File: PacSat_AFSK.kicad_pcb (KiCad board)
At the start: 6 copper layers, 92 x 92 mm, 308 parts, among them J10 2118718-2, J11 Molex 73251-1153, J2 CONN_02X05, J3 2118714-2, J4 2118714-2, J5 2118714-2, J6 2118714-2, J7 2118714-2, J8 Molex 73251-1153, J9 2118714-2, P10 CONUFL001-SMD-T, P11 CONUFL001-SMD-T, P12 CONUFL001-SMD-T, P13 CONUFL001-SMD-T, P14 Conn_04x26_Pin, P2 CONUFL001-SMD-T, P3 CONUFL001-SMD-T, P4 CONUFL001-SMD-T, P5 CONUFL001-SMD-T, P6 CONUFL001-SMD-T, P7 CONUFL001-SMD-T, P9 CONUFL001-SMD-T, Q2 BSS138, Q3 DMP2037U, Q4 DMP2037U, Q5 DMP2037U, Q6 DMP2037U, Q7 DMP2037U, U10 MAX4495AAUT, U11 MAX4495AAUT, U12 MAX31331TETB+, U13 AS1016204-0108X0PWAY, U14 TCAN1044ADDFRQ1, U15 AX5043, U17 AX5043, U19 AX5043, U2 TMS570LS0914PGE, U21 AX5043, U23 AX5043, U25 QPL9547, U26 RBP-140+, U27 TQP7M9106, U28 ADL5501AKSZ-R2, U29 ADL5501AKSZ-R2, U3 CDCLVC1106, U4 TPSM828302ARDSR, U5 LP3962EMP-3.3/NOPB, U6 STWD100NYWY3F, U8 MP5073GG-P, U9 MAX4495AAUT, Y2 O 16,0-JT22CT-A-P-3,3-LF, Y3 32.768kHz

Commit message: Remove the ground from KELVIN_GND
From reading the data sheet, it appears it is not supposed to be
connected.

Signed-off-by: Corey Minyard <corey@minyard.net>
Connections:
- U2 pad 19: GND -> unconnected-(U2-KELVIN_GND-Pad19)
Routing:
- net GND: track 291.5 -> 289.5 mm, vias 384 -> 383
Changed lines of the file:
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@@
 	(net 375 "AX5043_SEL1_N")
 	(net 376 "AX5043_SEL_TX_N")
+	(net 377 "unconnected-(U2-KELVIN_GND-Pad19)")
 	(footprint "Capacitor_SMD:C_0603_1608Metric_Pad1.08x0.95mm_HandSolder"
 		(layer "F.Cu")
@@
 			(size 1.6 0.3)
 			(layers "F.Cu" "F.Mask" "F.Paste")
-			(net 1 "GND")
+			(net 377 "unconnected-(U2-KELVIN_GND-Pad19)")
 			(pinfunction "KELVIN_GND")
-			(pintype "passive")
+			(pintype "passive+no_connect")
 		)
 		(pad "20" smd rect
@@
 	)
 	(segment
-		(start 190.758 77.715)
-		(end 190.758 79.7012)
-		(width 0.3048)
-		(layer "F.Cu")
-		(net 1)
-	)
-	(segment
 		(start 206.64 99.25)
 		(end 206.44 99.05)
@@
 		(size 0.508)
 		(drill 0.3048)
-		(layers "F.Cu" "B.Cu")
-		(net 1)
-	)
-	(via
-		(at 190.758 79.7012)
-		(size 0.508)
-		(drill 0.3048)

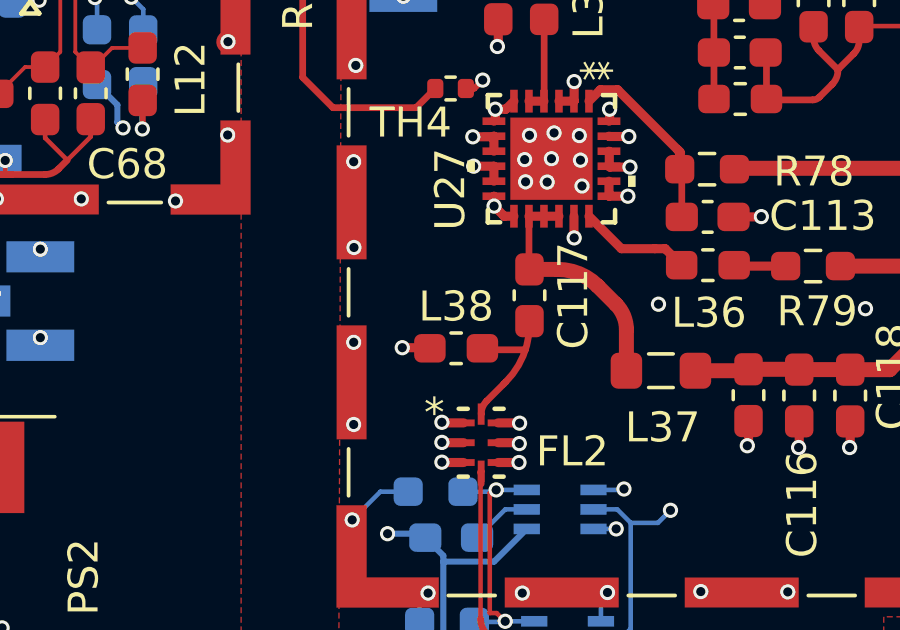
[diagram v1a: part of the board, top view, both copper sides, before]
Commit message: Check over notes and some component values
Fix a wrong capacitor in one spot, set Q and voltage as necessary.

Signed-off-by: Corey Minyard <corey@minyard.net>
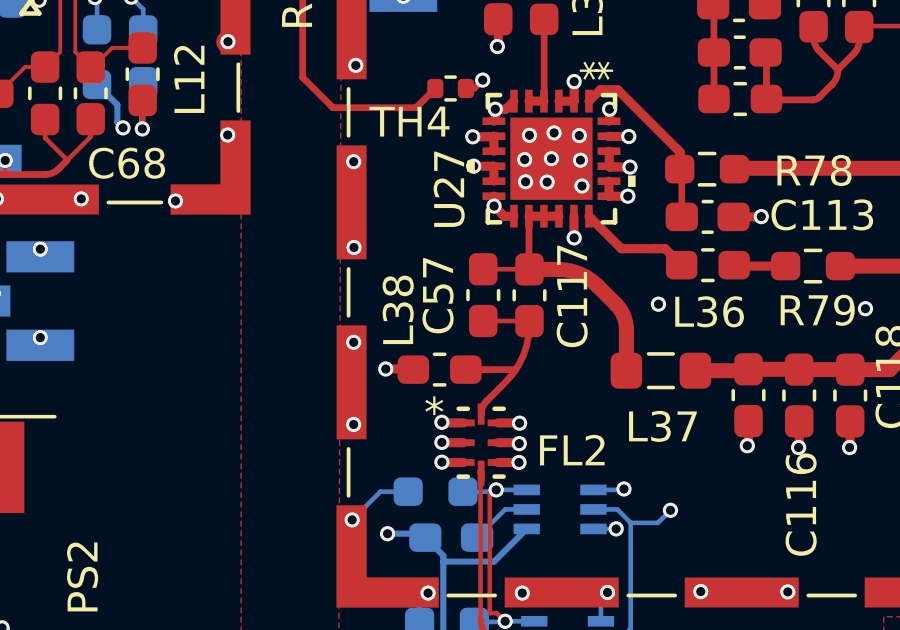
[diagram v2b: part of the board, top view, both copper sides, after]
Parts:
- added C57: 4p 1% 30V, Capacitor_SMD:C_0603_1608Metric_Pad1.08x0.95mm_HandSolder, F.Cu at (215.9, 129.3)
- C114: value 37p -> 37p 1%
- C117: value 60p -> 110p 1% 30V
- C88: value 5p1 -> 5p1 1%
- C89: value 11p -> 11p 1%
- C90: value 5p6 -> 5p6 1%
- C91, C92: value 4p3 -> 4p3 1%
- L15, L16: value 78n -> 78n 2% Q=28
- L17: value 1n -> 1n Q=12
- L20, L21: value 27n -> 27n 2% Q=40
- L22, L23: value 43n -> 43n 2% Q=40
- L35: value 17n -> 17n 2% Q>=40
- L38: value 6.9n -> 6.8n 2% Q=40
- moved L38 0.90 mm to (214.5, 131.8)
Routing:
- net Net-(FL2-INPUT): track 5.06 -> 6.86 mm
- net Net-(C117-Pad1): track 8.33 -> 9.87 mm

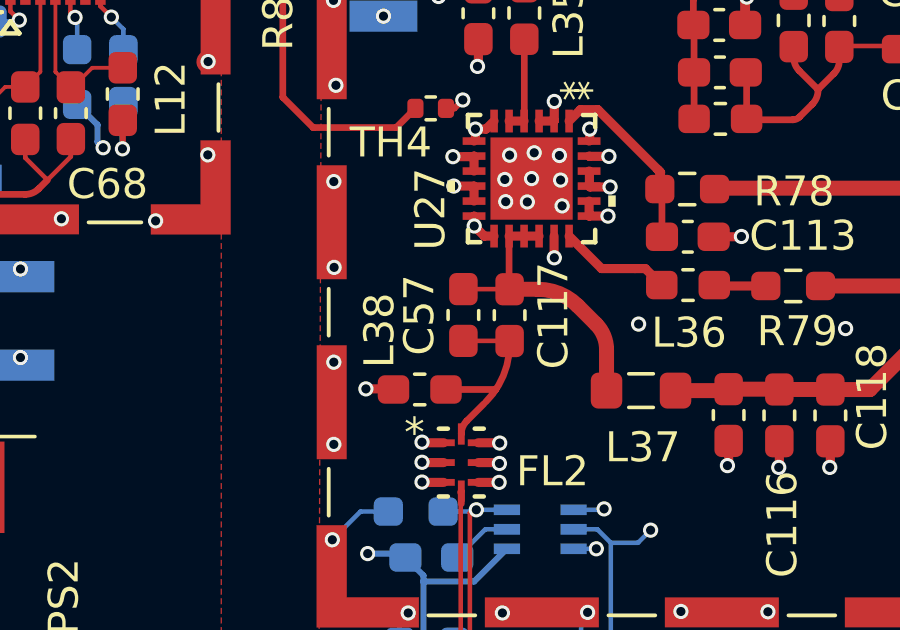
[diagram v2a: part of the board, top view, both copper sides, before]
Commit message: Adjust the TX output impedance match some more
Signed-off-by: Corey Minyard <corey@minyard.net>
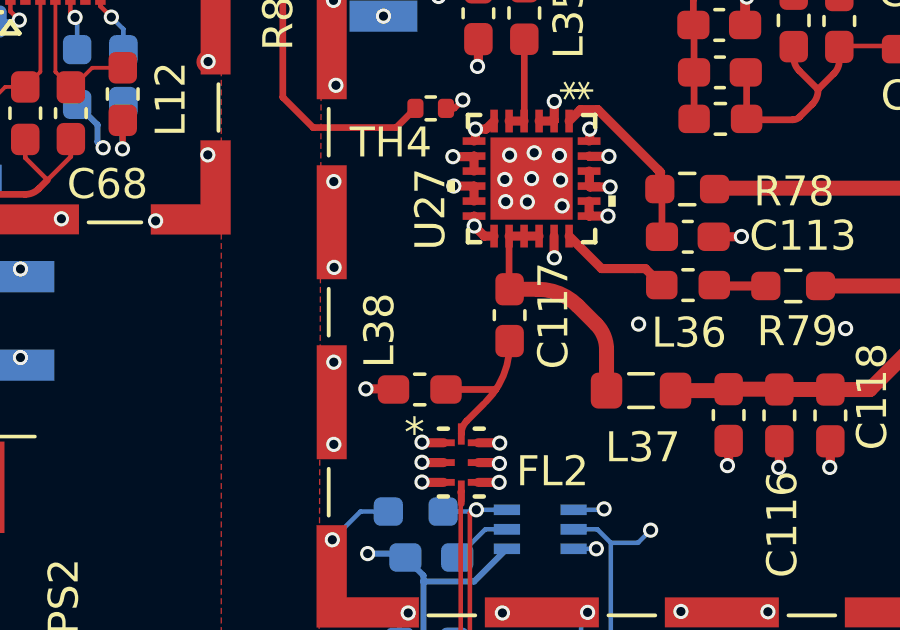
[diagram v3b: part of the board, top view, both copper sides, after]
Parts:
- removed C57: 4p 1% 30V, Capacitor_SMD:C_0603_1608Metric_Pad1.08x0.95mm_HandSolder
- C117: value 110p 1% 30V -> 130p 1% 30V
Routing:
- net Net-(FL2-INPUT): track 6.86 -> 5.32 mm
- net Net-(C117-Pad1): track 9.87 -> 8.34 mm
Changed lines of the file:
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@@
 		)
 	)
-	(footprint "Capacitor_SMD:C_0603_1608Metric_Pad1.08x0.95mm_HandSolder"
-		(layer "F.Cu")
-		(at 215.91 129.277499 -90)
-		(descr "Capacitor SMD 0603 (1608 Metric), square (rectangular) end terminal, IPC-7351 nominal with elongated pad for handsoldering. (Body size source: IPC-SM-782 page 76, https://www.pcb-3d.com/wordpress/wp-content/uploads/ipc-sm-782a_amendment_1_and_2.pdf), generated with kicad-footprint-generator")
-		(tags "capacitor handsolder")
-		(property "Reference" "C57"
-			(at 0 1.47 90)
-			(layer "F.SilkS")
-			(effects
-				(font
-					(size 1 1)
-					(thickness 0.15)
-				)
-			)
-		)
-		(property "Value" "4p 1% 30V"
-			(at 0 1.43 90)
-			(layer "F.Fab")
-			(effects
-				(font
-					(size 1 1)
-					(thickness 0.15)
-				)
-			)
-		)
-		(property "Datasheet" "~"
-			(at 0 0 90)
-			(layer "F.Fab")
-			(hide yes)
-			(effects
-				(font
-					(size 1.27 1.27)
-					(thickness 0.15)
-				)
-			)
-		)
-		(property "Description" ""
-			(at 0 0 90)
-			(layer "F.Fab")
-			(hide yes)
-			(effects
-				(font
-					(size 1.27 1.27)
-					(thickness 0.15)
-				)
-			)
-		)
-		(property ki_fp_filters "C_*")
-		(sheetname "/RF_Power_AMP_FET/")
-		(sheetfile "Power_Amp.kicad_sch")
-		(attr smd)
-		(fp_line
-			(start -0.146267 0.51)
-			(end 0.146267 0.51)
-			(stroke
-				(width 0.12)
-				(type solid)
-			)
-			(layer "F.SilkS")
-		)
-		(fp_line
-			(start -0.146267 -0.51)
-			(end 0.146267 -0.51)
-			(stroke
-				(width 0.12)
-				(type solid)
-			)
-			(layer "F.SilkS")
-		)
-		(fp_line
-			(start -1.65 0.73)
-			(end -1.65 -0.73)
-			(stroke
-				(width 0.05)
-				(type solid)
-			)
-			(layer "F.CrtYd")
-		)
-		(fp_line
-			(start 1.65 0.73)
-			(end -1.65 0.73)
-			(stroke
-				(width 0.05)
-				(type solid)
-			)
-			(layer "F.CrtYd")
-		)
-		(fp_line
-			(start -1.65 -0.73)
-			(end 1.65 -0.73)
-			(stroke
-				(width 0.05)
-				(type solid)
-			)
-			(layer "F.CrtYd")
-		)
-		(fp_line
-			(start 1.65 -0.73)
-			(end 1.65 0.73)
-			(stroke
-				(width 0.05)
-				(type solid)
-			)
-			(layer "F.CrtYd")
-		)
-		(fp_line
-			(start -0.8 0.4)
-			(end -0.8 -0.4)
-			(stroke
-				(width 0.1)
-				(type solid)
-			)
-			(layer "F.Fab")
-		)
-		(fp_line
-			(start 0.8 0.4)
-			(end -0.8 0.4)
-			(stroke
-				(width 0.1)
-				(type solid)
-			)
-			(layer "F.Fab")
-		)
-		(fp_line
-			(start -0.8 -0.4)
-			(end 0.8 -0.4)
-			(stroke
-				(width 0.1)
-				(type solid)
-			)
-			(layer "F.Fab")
-		)
-		(fp_line
-			(start 0.8 -0.4)
-			(end 0.8 0.4)
-			(stroke
-				(width 0.1)
-				(type solid)
-			)
-			(layer "F.Fab")
-		)
-		(fp_text user "${REFERENCE}"
-			(at 0 0 90)
-			(layer "F.Fab")
-			(effects
-				(font
-					(size 0.4 0.4)
-					(thickness 0.06)
-				)
-			)
-		)
-		(pad "1" smd roundrect
-			(at -0.862501 0 270)
-			(size 1.075 0.95)
-			(layers "F.Cu" "F.Mask" "F.Paste")
-			(roundrect_rratio 0.25)
-			(net 124 "Net-(C117-Pad1)")
-			(pintype "passive")
-		)
-		(pad "2" smd roundrect
-			(at 0.862501 0 270)
-			(size 1.075 0.95)
-			(layers "F.Cu" "F.Mask" "F.Paste")
-			(roundrect_rratio 0.25)
-			(net 134 "Net-(FL2-INPUT)")
-			(pintype "passive")
-		)
-		(embedded_fonts no)
-		(model "${KICAD9_3DMODEL_DIR}/Capacitor_SMD.3dshapes/C_0603_1608Metric.step"
-			(offset
-				(xyz 0 0 0)
-			)
-			(scale
-				(xyz 1 1 1)
-			)
-			(rotate
-				(xyz 0 0 0)
-			)
-		)
-	)
 	(footprint "Resistor_SMD:R_0603_1608Metric_Pad0.98x0.95mm_HandSolder"
 		(layer "F.Cu")
@@
 			)
 		)
-		(property "Value" "110p 1% 30V"
+		(property "Value" "130p 1% 30V"
 			(at 0 1.43 90)
 			(layer "F.Fab")
@@
 	)
 	(segment
-		(start 215.91 128.414998)
-		(end 217.444998 128.414998)
-		(width 0.1524)
-		(layer "F.Cu")
-		(net 124)
-	)
-	(segment
 		(start 217.9323 126.6477)
 		(end 217.432299 126.6477)
@@
 		(layer "F.Cu")
 		(net 134)
-	)
-	(segment
-		(start 215.91 130.14)
-		(end 217.445 130.14)
-		(width 0.1524)
-		(layer "F.Cu")
-		(net 134)

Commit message: More work on the LNA/PA impedance matchers
Did some simulations, found some issues.

Signed-off-by: Corey Minyard <corey@minyard.net>
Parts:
- C104: value 13p 1% -> 6.4p 1%
- C110: value 11p 1% -> 580p 2%
- C114: value 37p 1% -> 39p 1%
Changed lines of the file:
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@@
 			)
 		)
-		(property "Value" "13p 1%"
+		(property "Value" "6.4p 1%"
 			(at 0 1.16 0)
 			(layer "F.Fab")
@@
 			)
 		)
-		(property "Value" "11p 1%"
+		(property "Value" "580p 2%"
 			(at 0 1.16 0)
 			(layer "F.Fab")
@@
 			)
 		)
-		(property "Value" "37p 1%"
+		(property "Value" "39p 1%"
 			(at 0 1.43 90)
 			(layer "F.Fab")
